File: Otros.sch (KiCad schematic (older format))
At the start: 8 parts, among them U4 ADP150, U5 ASFLMB-16.000MHZ-LY-T

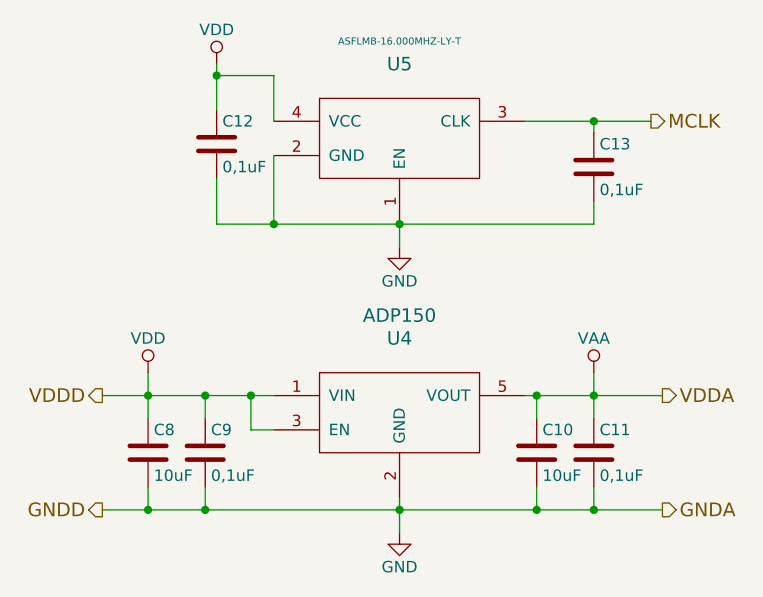
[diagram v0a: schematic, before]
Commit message: Ruteados los conjuntos por separado
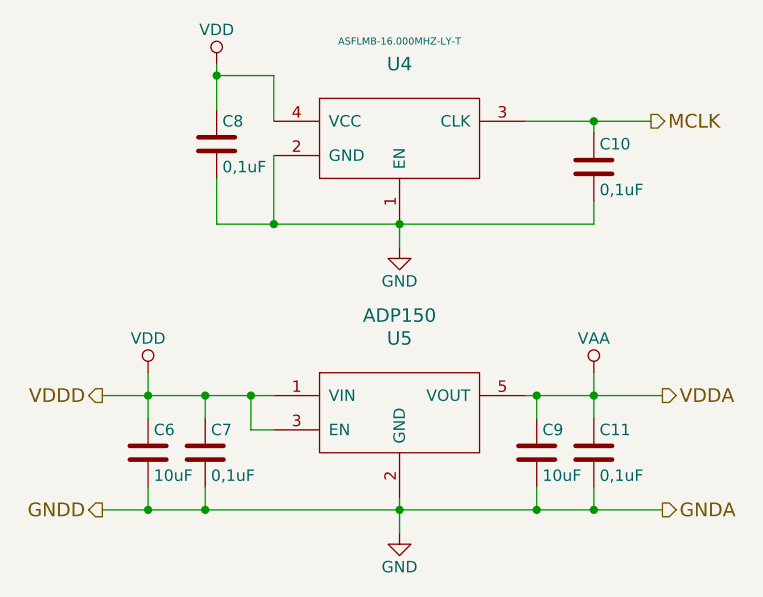
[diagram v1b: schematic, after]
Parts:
- renumbered C13 to C10, C8 to C6, C9 to C7, C12 to C8, C10 to C9, U5 to U4, U4 to U5
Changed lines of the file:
@@
 GNDA
 $Comp
-L ADP150 U4
+L ADP150 U5
 U 1 1 582F5A80
 P 6350 2700
-F 0 "U4" H 6350 3000 59  0000 C CNN
+F 0 "U5" H 6350 3000 59  0000 C CNN
 F 1 "ADP150" H 6350 3100 59  0000 C CNN
 F 2 "TO_SOT_Packages_SMD:SC-70-5" H 6350 2700 59  0001 C CNN
@@
 	6900 2650 7500 2650
 $Comp
-L C C8
+L C C6
 U 1 1 582F5B1F
 P 5250 2900
-F 0 "C8" H 5275 3000 50  0000 L CNN
+F 0 "C6" H 5275 3000 50  0000 L CNN
 F 1 "10uF" H 5275 2800 50  0000 L CNN
 F 2 "Capacitors_SMD:C_0603" H 5288 2750 50  0001 C CNN
@@
 $EndComp
 $Comp
-L C C9
+L C C7
 U 1 1 582F5B72
 P 5500 2900
-F 0 "C9" H 5525 3000 50  0000 L CNN
+F 0 "C7" H 5525 3000 50  0000 L CNN
 F 1 "0,1uF" H 5525 2800 50  0000 L CNN
 F 2 "Capacitors_SMD:C_0603" H 5538 2750 50  0001 C CNN
@@
 $EndComp
 $Comp
-L C C10
+L C C9
 U 1 1 582F5BCF
 P 6950 2900
-F 0 "C10" H 6975 3000 50  0000 L CNN
+F 0 "C9" H 6975 3000 50  0000 L CNN
 F 1 "10uF" H 6975 2800 50  0000 L CNN
 F 2 "Capacitors_SMD:C_0603" H 6988 2750 50  0001 C CNN
@@
 MCLK
 $Comp
-L ASFLMB-16.000MHZ-LY-T U5
+L ASFLMB-16.000MHZ-LY-T U4
 U 1 1 5838BB55
 P 6350 1500
-F 0 "U5" H 6350 1800 59  0000 C CNN
+F 0 "U4" H 6350 1800 59  0000 C CNN
 F 1 "ASFLMB-16.000MHZ-LY-T" H 6350 1900 31  0000 C CNN
 F 2 "propios:TCXO" H 6350 1500 59  0001 C CNN
@@
 $EndComp
 $Comp
-L C C12
+L C C8
 U 1 1 5838BB5C
 P 5550 1550
-F 0 "C12" H 5575 1650 50  0000 L CNN
+F 0 "C8" H 5575 1650 50  0000 L CNN
 F 1 "0,1uF" H 5575 1450 50  0000 L CNN
 F 2 "Capacitors_SMD:C_0603" H 5588 1400 50  0001 C CNN
@@
 $EndComp
 $Comp
-L C C13
+L C C10
 U 1 1 5838BB63
 P 7200 1650
-F 0 "C13" H 7225 1750 50  0000 L CNN
+F 0 "C10" H 7225 1750 50  0000 L CNN
 F 1 "0,1uF" H 7225 1550 50  0000 L CNN
 F 2 "Capacitors_SMD:C_0603" H 7238 1500 50  0001 C CNN
